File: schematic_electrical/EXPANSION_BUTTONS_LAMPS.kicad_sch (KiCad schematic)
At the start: 4 parts, among them SW1 AB_800T-QT24, SW2 AB_800T-QT24, SW3 AB_800T-QT24, SW4 AB_800T-QT24

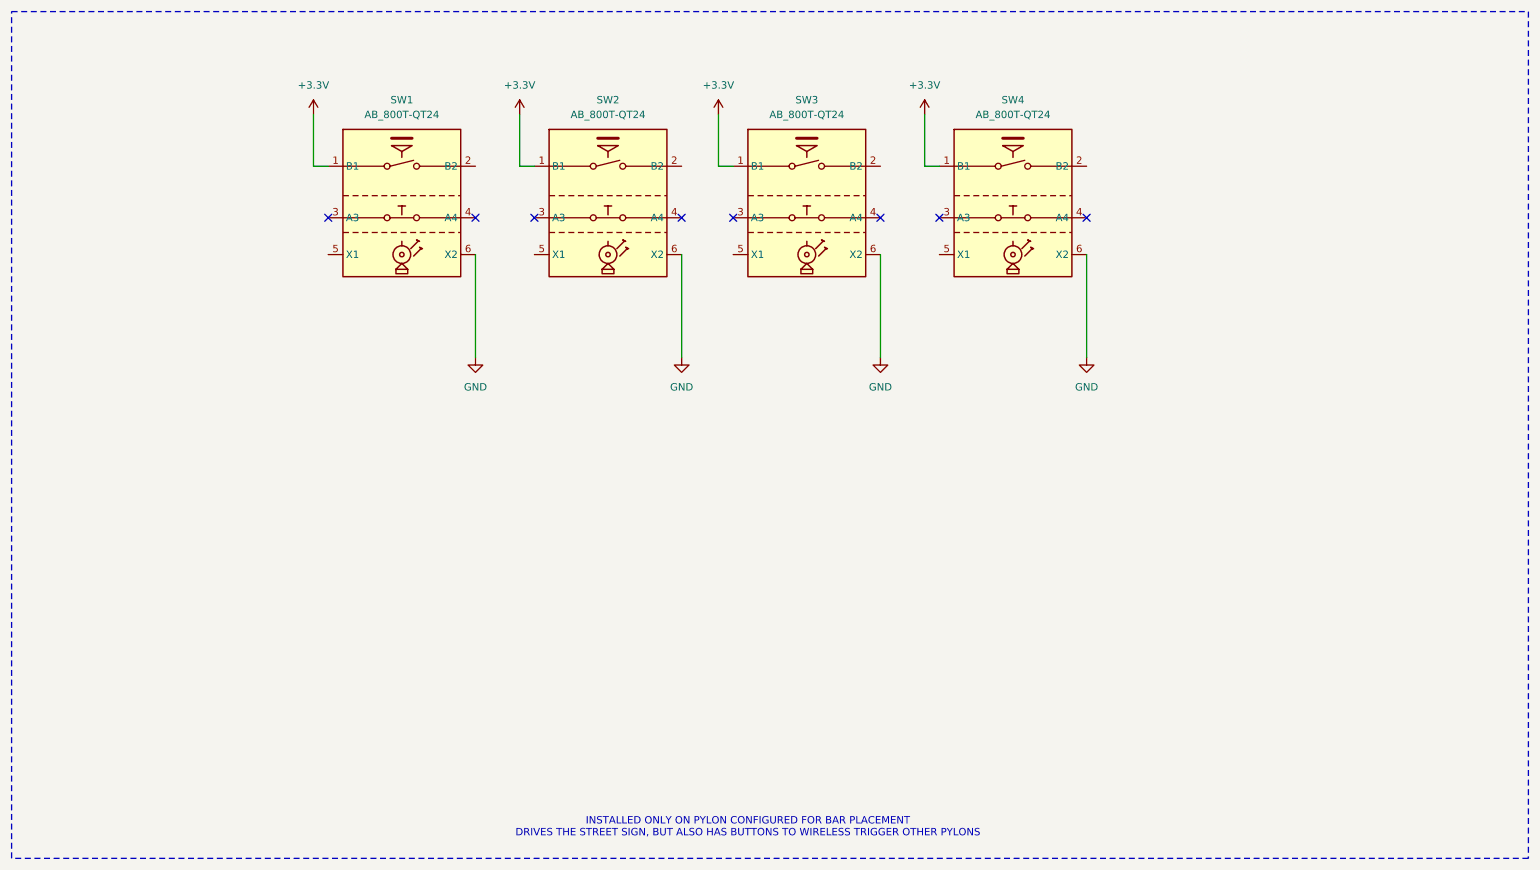
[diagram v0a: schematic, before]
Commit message: Schematic options for bar placement bar box (button controller)
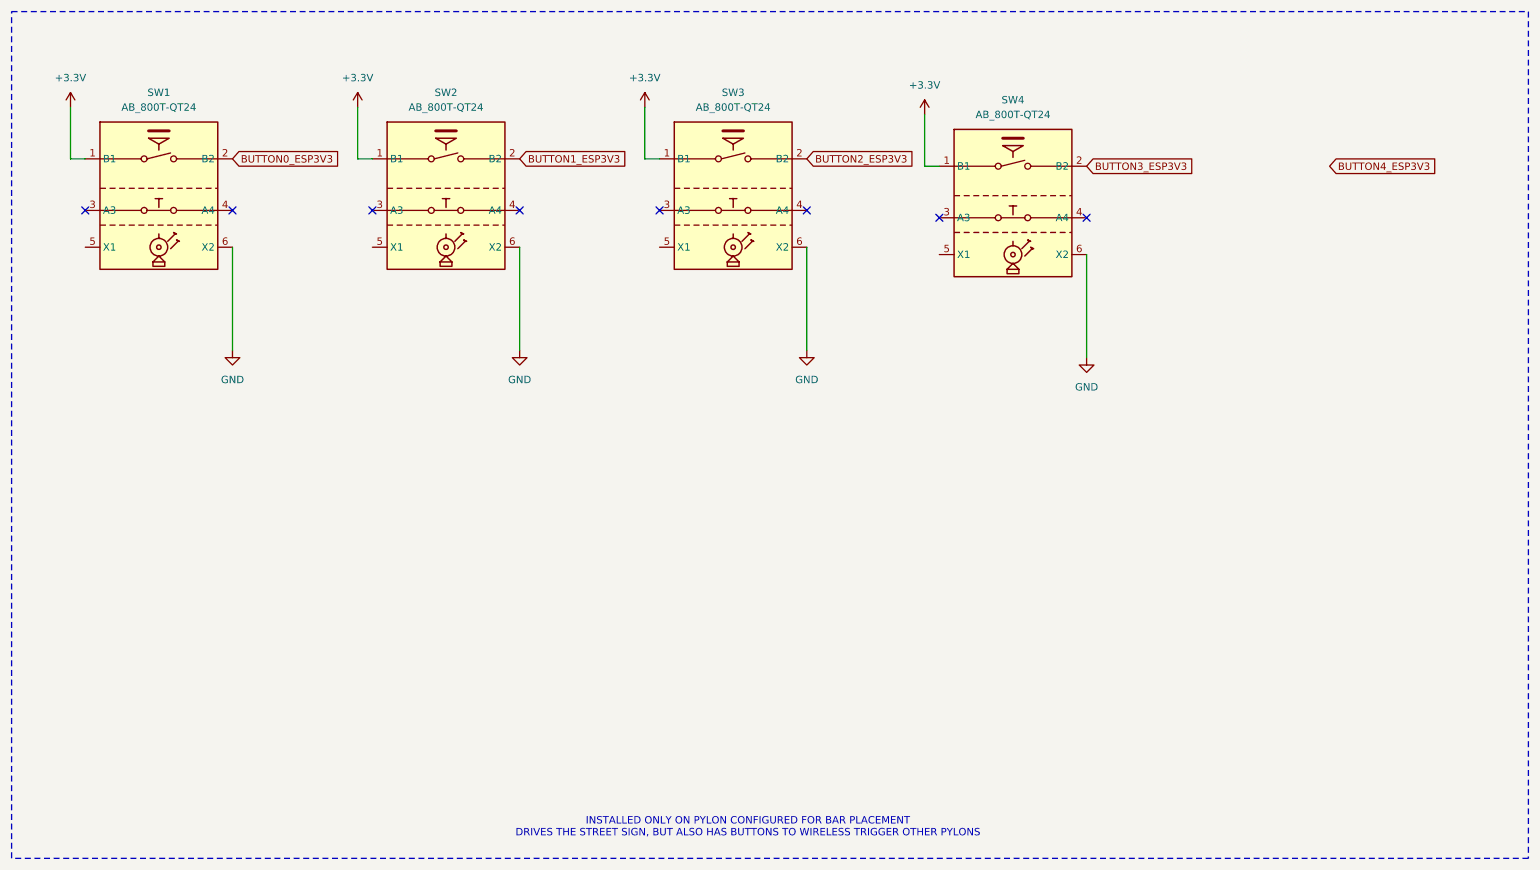
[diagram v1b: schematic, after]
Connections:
- net BUTTON3_ESP3V3: now reaches SW4.2 (B2)
- net BUTTON2_ESP3V3: now reaches SW3.2 (B2)
- net BUTTON1_ESP3V3: now reaches SW2.2 (B2)
- net BUTTON0_ESP3V3: now reaches SW1.2 (B2)
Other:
- moved on the sheet: SW1, SW2, SW3

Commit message: delete button4
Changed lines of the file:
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@@
-		)
-	)
-	(global_label "BUTTON4_ESP3V3"
-		(shape input)
-		(at 243.84 43.18 0)
-		(fields_autoplaced yes)
-		(effects
-			(font
-				(size 1.27 1.27)
-			)
-			(justify left)
-		)
-		(property "Intersheetrefs" "${INTERSHEET_REFS}"
-			(at 255.2314 43.18 0)
-			(effects
-				(font
-					(size 1.27 1.27)
-				)
-				(justify left)
-				(hide yes)
-			)
 		)
 	)

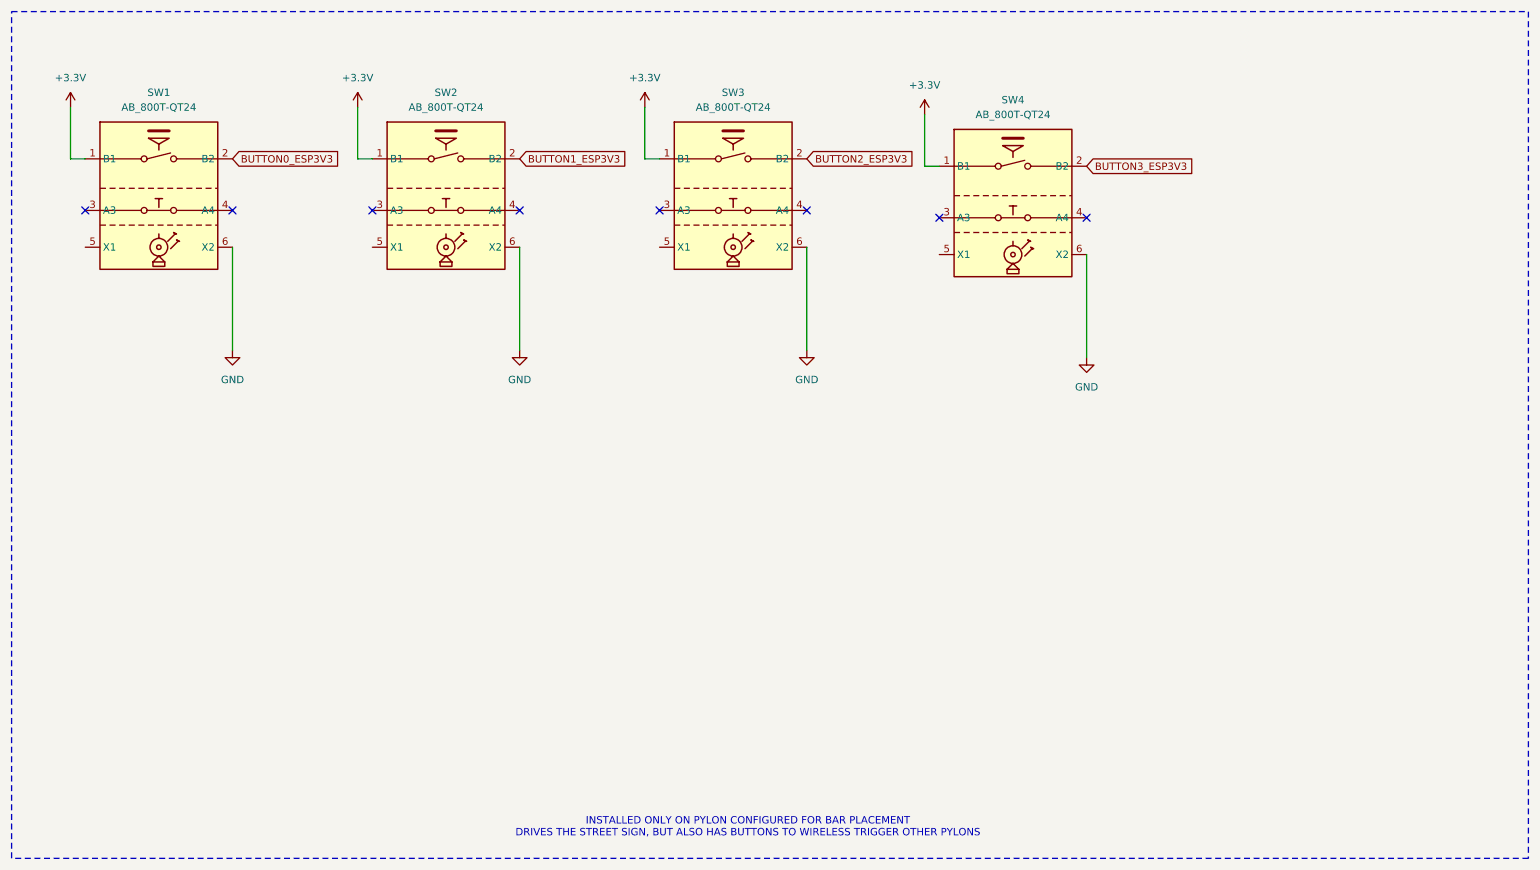
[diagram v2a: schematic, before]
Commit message: Schematic for bar: use ULN2308 for button 12V lamps
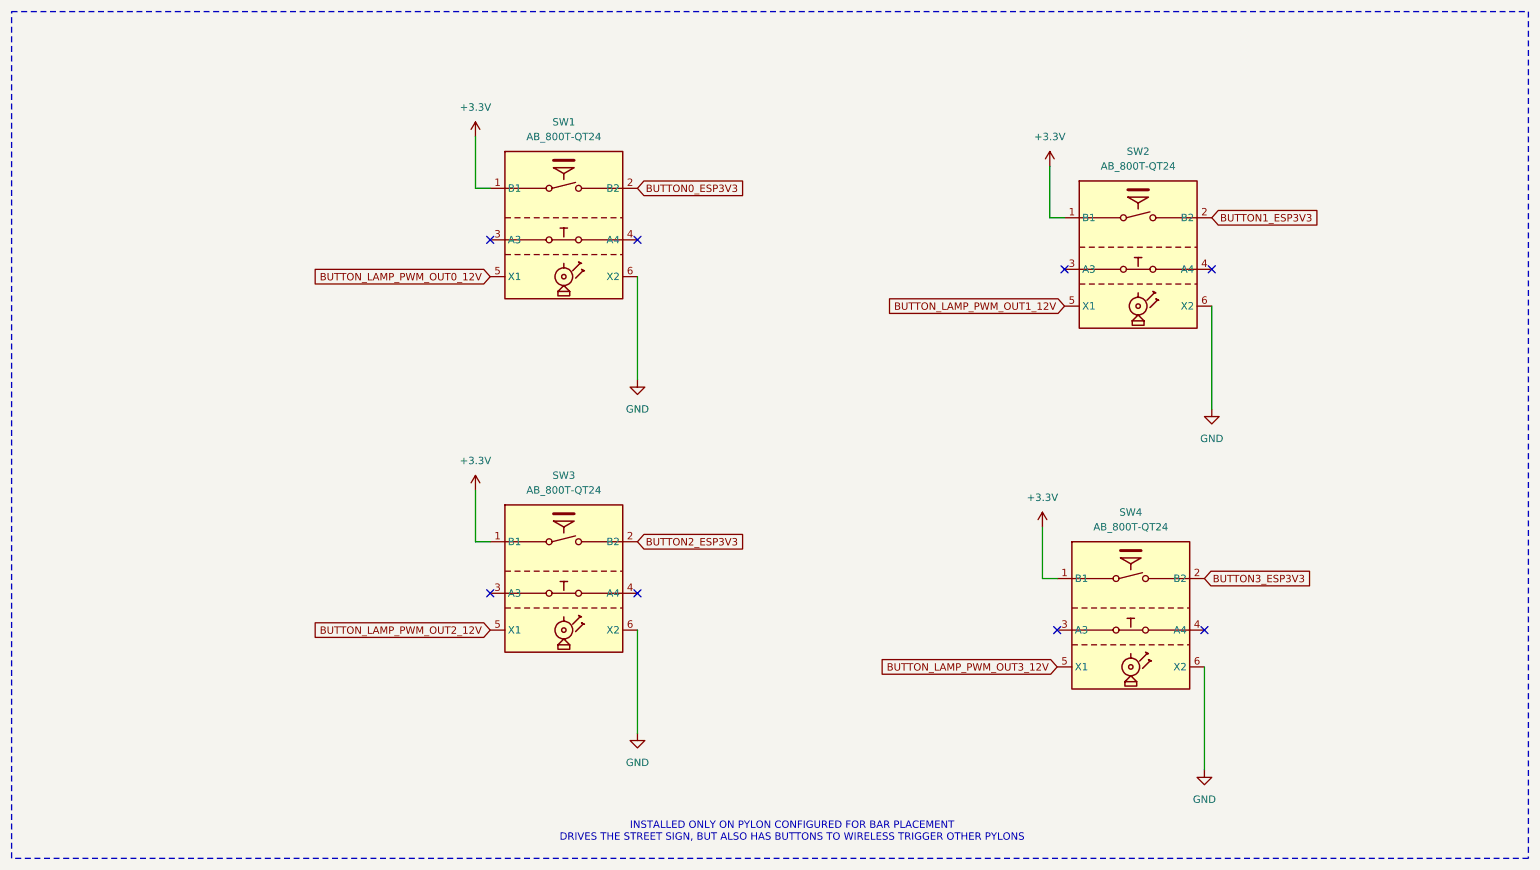
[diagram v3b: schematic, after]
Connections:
- net BUTTON_LAMP_PWM_OUT3_12V: now reaches SW4.5 (X1)
- net BUTTON_LAMP_PWM_OUT2_12V: now reaches SW3.5 (X1)
- net BUTTON_LAMP_PWM_OUT1_12V: now reaches SW2.5 (X1)
- net BUTTON_LAMP_PWM_OUT0_12V: now reaches SW1.5 (X1)
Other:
- moved on the sheet: SW1, SW2, SW3, SW4

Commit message: Schematic as built for bar box. 12V fire enable switch wired in correct manner such that LED is off when switch is off.
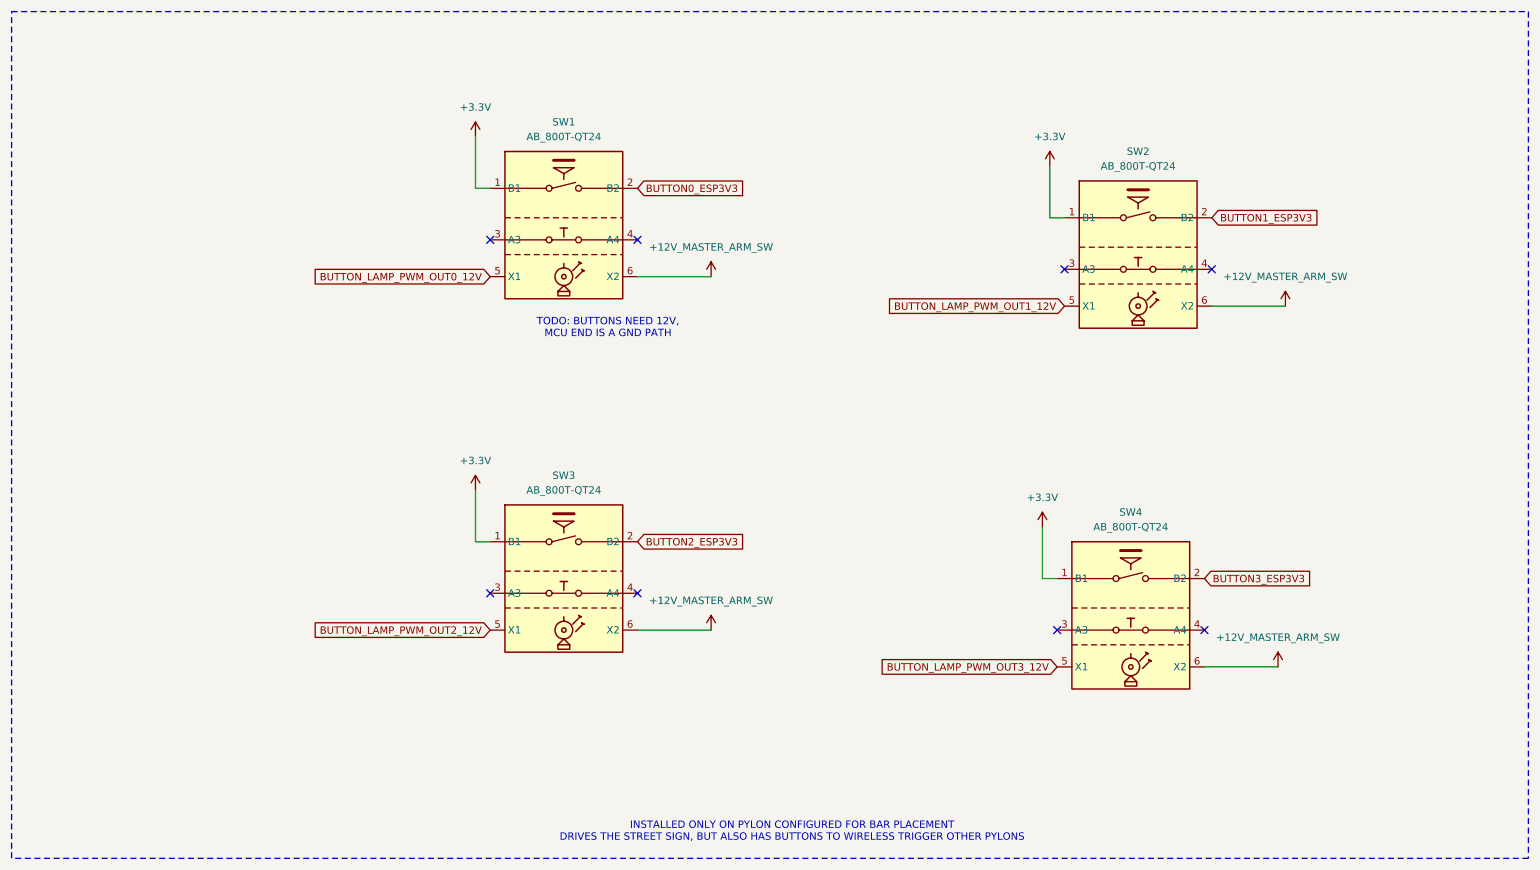
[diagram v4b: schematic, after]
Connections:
- net GND renamed +12V_MASTER_ARM_SW
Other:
- note added: "TODO: BUTTONS NEED 12V, MCU END IS A GND PATH"
